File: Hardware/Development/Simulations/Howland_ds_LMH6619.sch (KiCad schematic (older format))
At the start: 14 parts, among them U1 OPAMP, U2 OPAMP

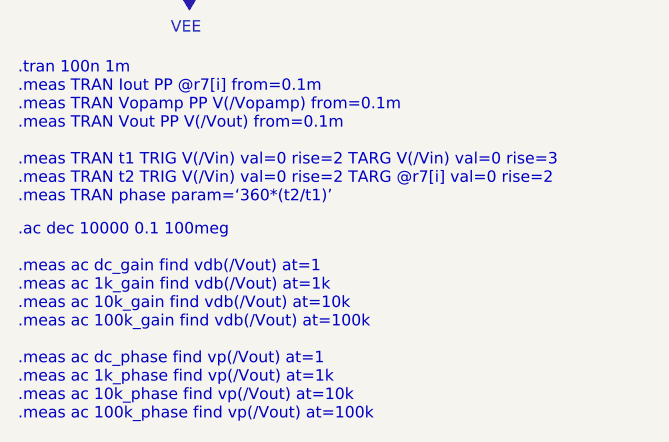
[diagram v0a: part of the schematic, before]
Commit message: Fixed error in IQ mode (2)
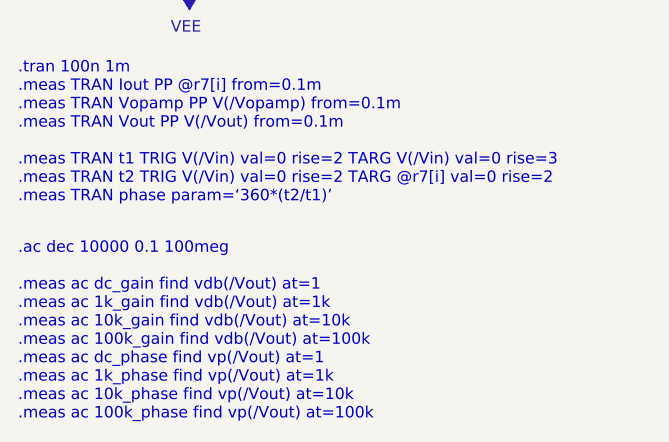
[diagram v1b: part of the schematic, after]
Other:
- note added: ".ac dec 10000 0.1 100meg \n\n.meas ac dc_gain find vdb(/Vout) at=1\n.meas ac 1k_gain find vdb(/Vout) at=1k\n.meas ac 10k_gain find vdb(/Vout) at=10k\n.meas ac 100k_gain find vdb(/Vout) at=100k​\n.meas ac dc_phase find vp(/Vout) at=1\n.meas ac 1k_phase find vp(/Vout) at=1k\n.meas ac 10k_phase find vp(/Vout) at=10k\n.meas ac 100k_phase find vp(/Vout) at=100k"
- note removed: ".ac dec 10000 0.1 100meg \n\n.meas ac dc_gain find vdb(/Vout) at=1\n.meas ac 1k_gain find vdb(/Vout) at=1k\n.meas ac 10k_gain find vdb(/Vout) at=10k\n.meas ac 100k_gain find vdb(/Vout) at=100k​\n\n.meas ac dc_phase find vp(/Vout) at=1\n.meas ac 1k_phase find vp(/Vout) at=1k\n.meas ac 10k_phase find vp(/Vout) at=10k\n.meas ac 100k_phase find vp(/Vout) at=100k"
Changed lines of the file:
@@
 $EndComp
 Text Notes 750  7900 0    50   ~ 0
-.ac dec 10000 0.1 100meg \n\n.meas ac dc_gain find vdb(/Vout) at=1\n.meas ac 1k_gain find vdb(/Vout) at=1k\n.meas ac 10k_gain find vdb(/Vout) at=10k\n.meas ac 100k_gain find vdb(/Vout) at=100k​\n\n.meas ac dc_phase find vp(/Vout) at=1\n.meas ac 1k_phase find vp(/Vout) at=1k\n.meas ac 10k_phase find vp(/Vout) at=10k\n.meas ac 100k_phase find vp(/Vout) at=100k
+.ac dec 10000 0.1 100meg \n\n.meas ac dc_gain find vdb(/Vout) at=1\n.meas ac 1k_gain find vdb(/Vout) at=1k\n.meas ac 10k_gain find vdb(/Vout) at=10k\n.meas ac 100k_gain find vdb(/Vout) at=100k​\n.meas ac dc_phase find vp(/Vout) at=1\n.meas ac 1k_phase find vp(/Vout) at=1k\n.meas ac 10k_phase find vp(/Vout) at=10k\n.meas ac 100k_phase find vp(/Vout) at=100k
 Wire Wire Line
 	7500 4300 7500 5000
